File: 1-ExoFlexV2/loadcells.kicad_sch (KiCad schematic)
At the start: 45 parts, among them J70 3,3k, J71 3,3k, J72 0Ω, J73 0Ω, J74 0Ω, J75 0Ω, U13 INA823DR, U14 INA823DR, U15 INA823DR, U19 SN74LVC1G32DBVR, U20 SN74LVC1G32DBVR

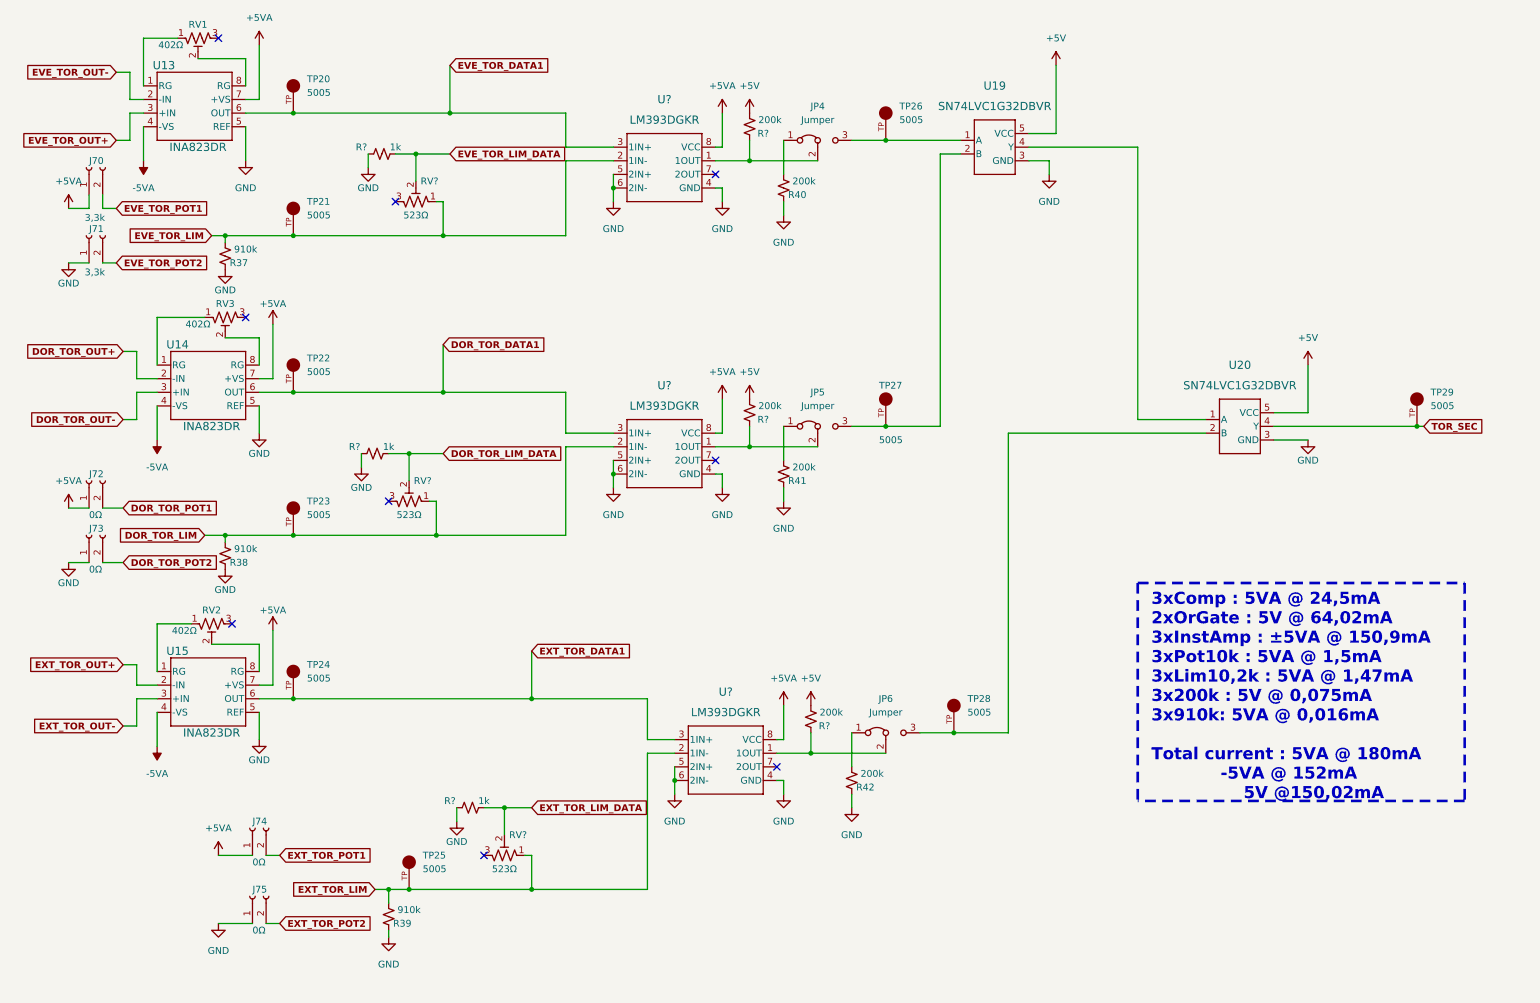
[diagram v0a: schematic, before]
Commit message: Chokes et RC
- Ajout des RF chokes
- Changement des résistance pour 0805
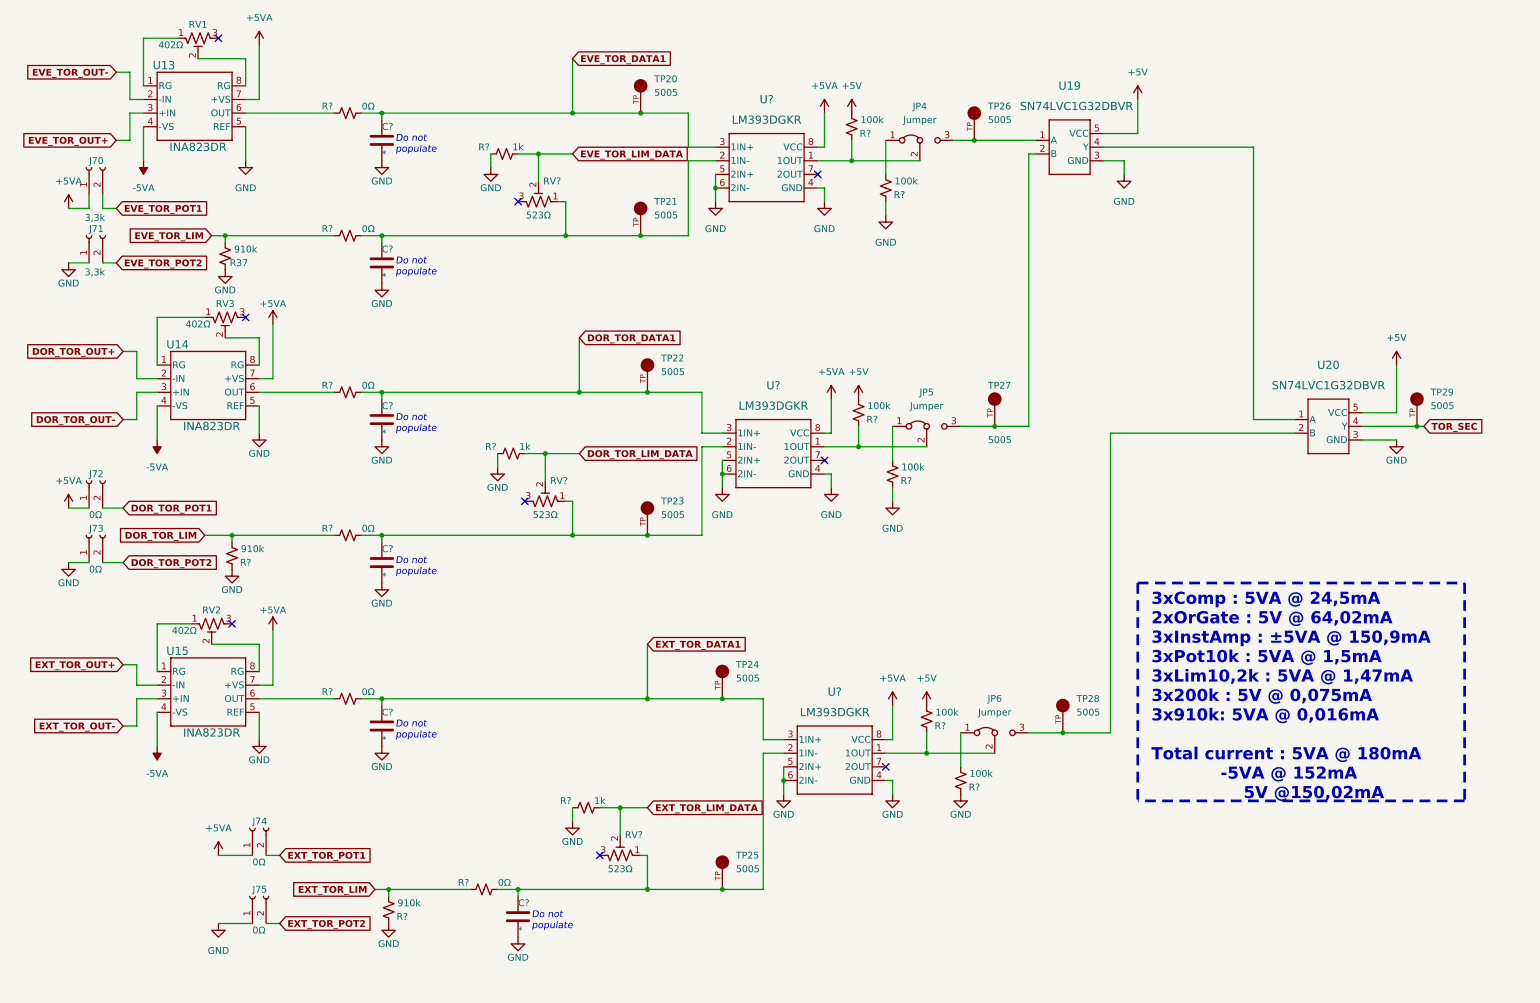
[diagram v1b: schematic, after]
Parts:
- removed R38, R39: 910k, Resistor_SMD:R_0603_1608Metric, symbol Device:R_Small_US
- removed R40, R41, R42, R? (x3): 200k, Resistor_SMD:R_0603_1608Metric, symbol Device:R_Small_US
- added C? (x6): *, Capacitor_SMD:C_0805_2012Metric, symbol Device:C
- added R? (x2): 910k, Resistor_SMD:R_0805_2012Metric, symbol Device:R_Small_US
- added R? (x6): 0Ω, Resistor_SMD:R_0805_2012Metric, symbol Device:R_Small_US
- added R? (x6): 100k, Resistor_SMD:R_0805_2012Metric, symbol Device:R_Small_US
- R37: footprint Resistor_SMD:R_0603_1608Metric -> Resistor_SMD:R_0805_2012Metric
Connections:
- net +5V: now also R?.1, R?.1, R?.1
- net DOR_TOR_DATA1: now also C?.1, R?.2; no longer U14.6 (OUT)
- net DOR_TOR_LIM: now also R?.1, R?.1; no longer RV?.1, TP23.TP, U?.2 (1IN-)
- net EVE_TOR_DATA1: now also C?.1, R?.2; no longer U13.6 (OUT)
- net EVE_TOR_LIM: now also R?.1; no longer RV?.1, TP21.TP, U?.2 (1IN-)
- net EXT_TOR_DATA1: now also C?.1, R?.2; no longer U15.6 (OUT)
- net EXT_TOR_LIM: now also R?.1, R?.1; no longer RV?.1, TP25.TP, U?.2 (1IN-)
- net GND: now also C?.2, C?.2, C?.2, C?.2, C?.2, C?.2, R?.2, R?.2, R?.2, R?.2, R?.2
- net at JP6.1 (A): now also R?.1
- net at JP6.2 (C), U?.1 (1OUT): now also R?.2
- net at JP4.1 (A): now also R?.1
- net at JP4.2 (C), U?.1 (1OUT): now also R?.2
- net at JP5.2 (C), U?.1 (1OUT): now also R?.2
- net at JP5.1 (A): now also R?.1
- new net: C?.1, R?.2, RV?.1, TP21.TP, U?.2 (1IN-)
- new net: R?.1, U14.6 (OUT)
- new net: C?.1, R?.2, RV?.1, TP23.TP, U?.2 (1IN-)
- new net: R?.1, U13.6 (OUT)
- new net: C?.1, R?.2, RV?.1, TP25.TP, U?.2 (1IN-)
- new net: R?.1, U15.6 (OUT)
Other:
- note added: "Do not populate"
- moved on the sheet: JP4, JP5, JP6, R?, RV?, TP20, TP21, TP22, TP23, TP24, TP25, TP26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

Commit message: Trimmer et jumper
-Changement de symbole de jumper
-Ajout des des trimmer aux endroits nécessaires
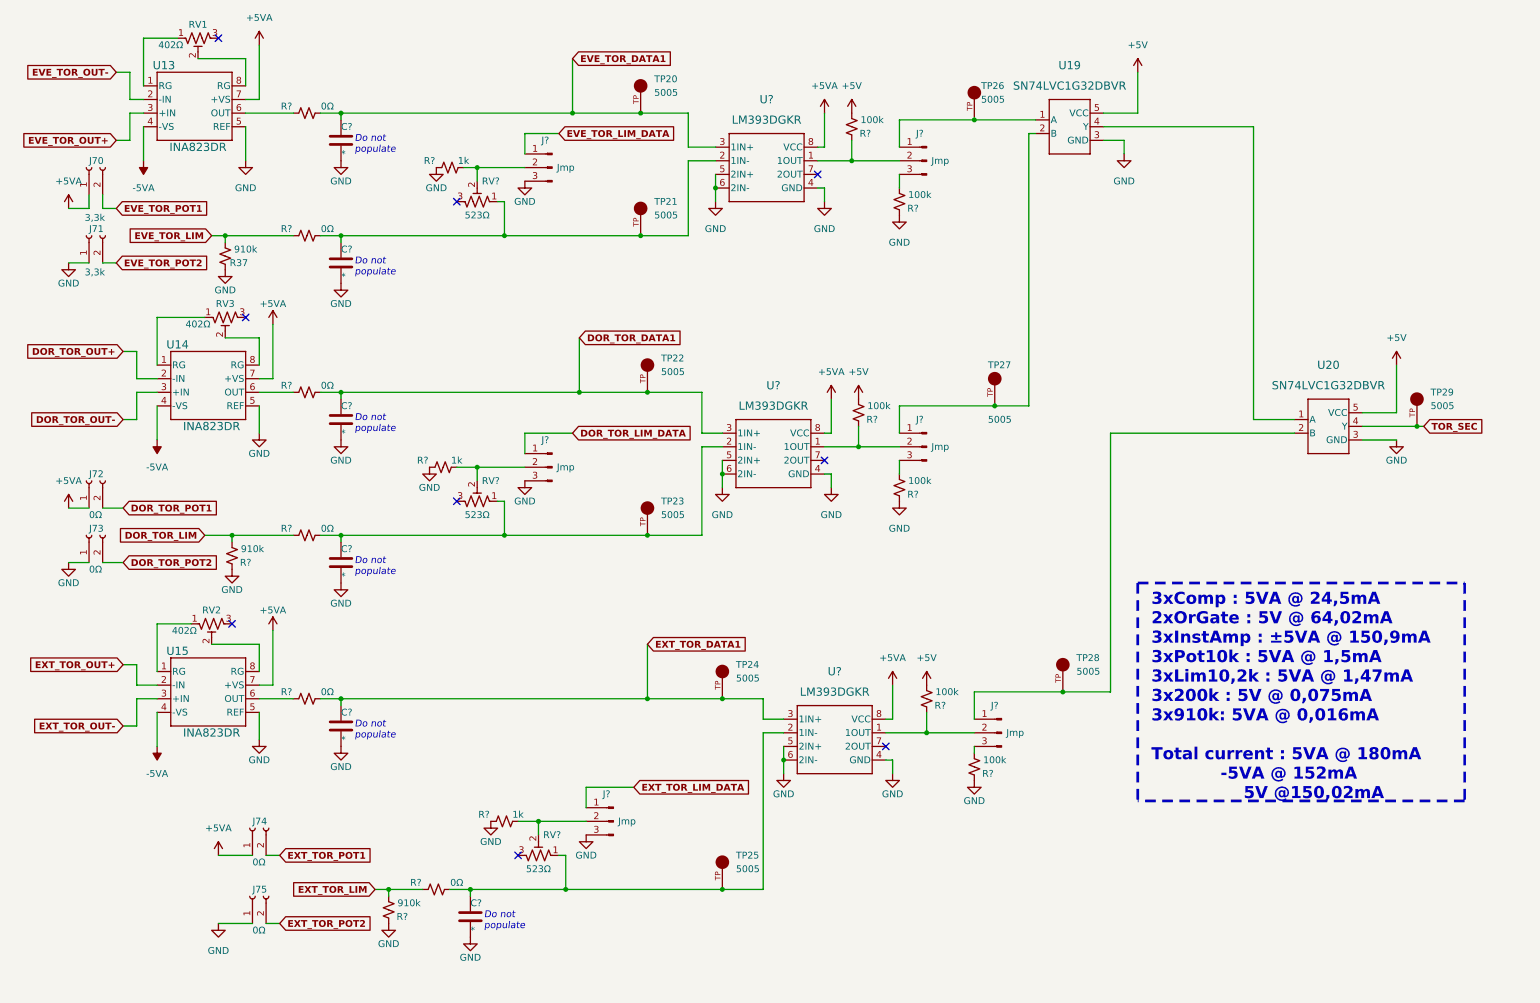
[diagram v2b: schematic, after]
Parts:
- removed JP4, JP5, JP6: Jumper, Connector_PinHeader_2.54mm:PinHeader_1x03_P2.54mm_Vertical, symbol Jumper:Jumper_3_Bridged12
- removed R? (x3): 100k, Resistor_SMD:R_0805_2012Metric, symbol Device:R_Small_US
- removed R?: 1k, Resistor_SMD:R_0805_2012Metric, symbol Device:R_Small_US
- removed RV?: 523Ω, FootPrint:TRIM_3362P-1-102LF, symbol Device:R_Potentiometer_Trim_US
- added J? (x6): Jmp, symbol Connector:Conn_01x03_Male
- added R?: 1k, Resistor_SMD:R_0805_2012Metric, symbol Device:R_Small_US
- added R? (x3): 100k, Resistor_SMD:R_0805_2012Metric, symbol Device:R_Small_US
- added RV?: 523Ω, FootPrint:TRIM_3362P-1-102LF, symbol Device:R_Potentiometer_Trim_US
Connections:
- net DOR_TOR_LIM_DATA: now also J?.1 (Pin_1); no longer R?.2, RV?.2
- net EVE_TOR_LIM_DATA: now also J?.1 (Pin_1); no longer R?.2, RV?.2
- net EXT_TOR_LIM_DATA: now also J?.1 (Pin_1)
- net GND: now also J?.3 (Pin_3), J?.3 (Pin_3), J?.3 (Pin_3), R?.1, R?.2, R?.2, R?.2
- net at TP27.TP, U19.2 (B): now also J?.1 (Pin_1)
- net at R?.2, U?.1 (1OUT): now also J?.2 (Pin_2) (x3)
- net at TP28.TP, U20.2 (B): now also J?.1 (Pin_1)
- net at C?.1, R?.2, TP25.TP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: now also RV?.1
- net at TP26.TP, U19.1 (A): now also J?.1 (Pin_1)
- new net: J?.2 (Pin_2), R?.2, RV?.2 (x3)
- new net: J?.3 (Pin_3), R?.1 (x3)
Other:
- moved on the sheet: C?, R?, RV?, TP26, TP27, TP28, U19, U?

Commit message: Test points et notes
- Ajout de tous les tests point nécessaires
-  Ajoute des sections de notes dans chaque page
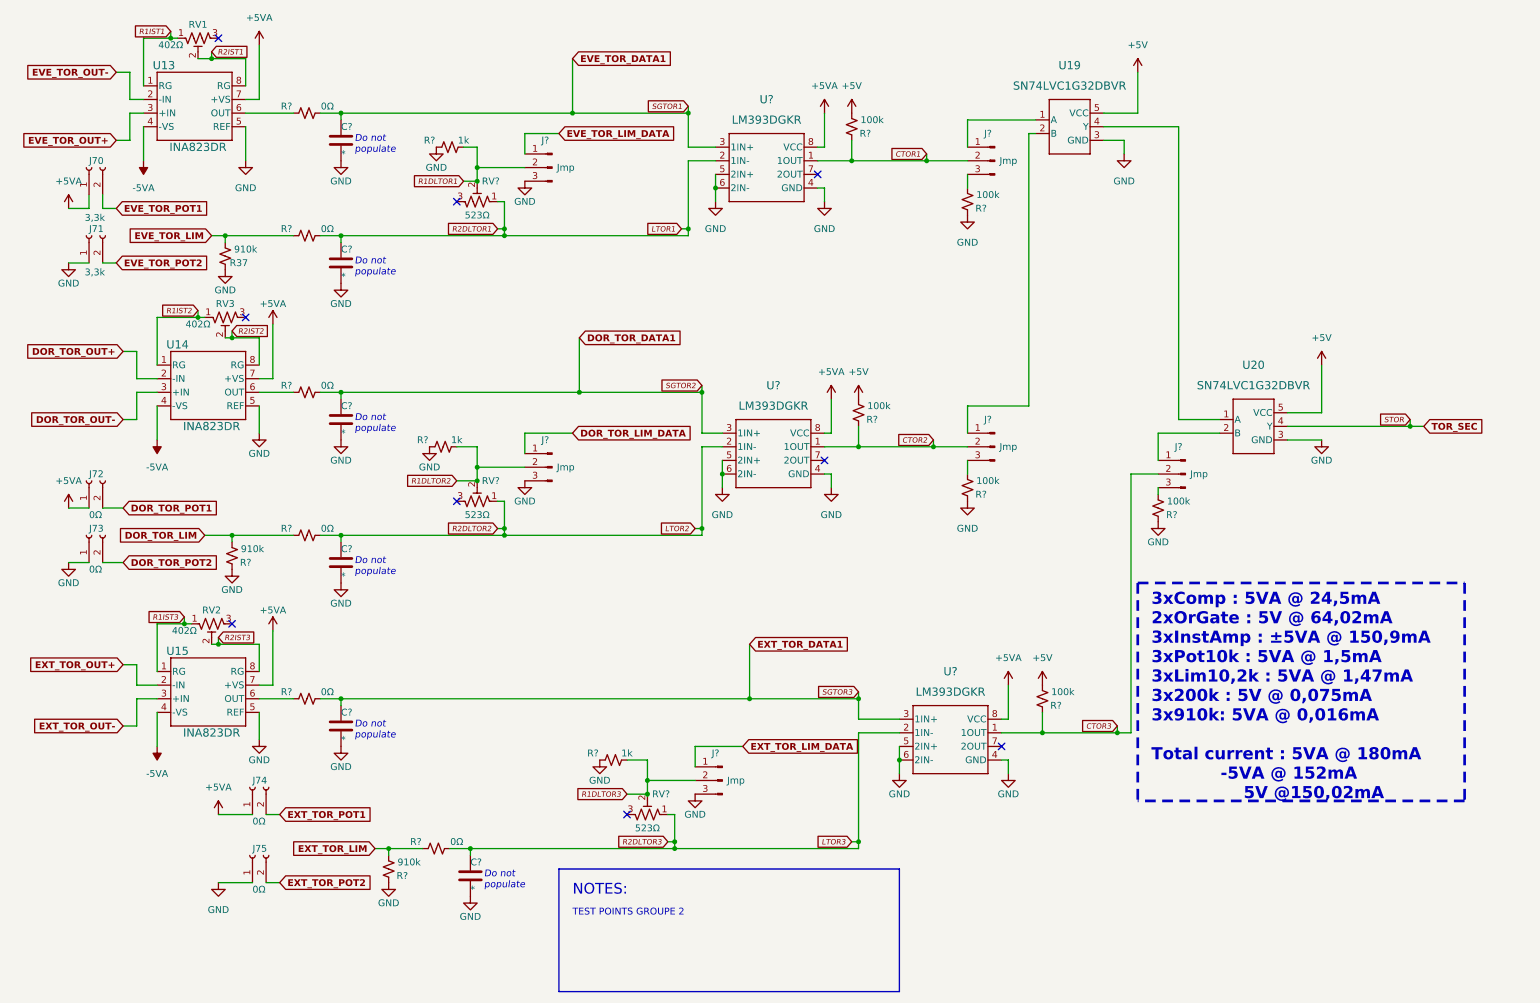
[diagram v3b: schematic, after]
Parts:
- removed TP20, TP21, TP22, TP23, TP24, TP25, TP26, TP27, TP28, TP29: 5005, FootPrint:KEYSTONE_5005, symbol SymLib:5005
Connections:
- net LTOR1: now reaches C?.1, R?.2, RV?.1, U?.2 (1IN-)
- net R1DLTOR1: now reaches J?.2 (Pin_2), R?.2, RV?.2
- net R1DLTOR3: now reaches J?.2 (Pin_2), R?.2, RV?.2
- net R1IST2: now reaches RV3.1, U14.1 (RG)
- net R2IST2: now reaches RV3.2, U14.8 (RG)
- net LTOR2: now reaches C?.1, R?.2, RV?.1, U?.2 (1IN-)
- net CTOR3: now reaches J?.2 (Pin_2), R?.2, U?.1 (1OUT)
- net R1IST1: now reaches RV1.1, U13.1 (RG)
- net R2IST1: now reaches RV1.2, U13.8 (RG)
- net LTOR3: now reaches C?.1, R?.2, RV?.1, U?.2 (1IN-)
- net R1DLTOR2: now reaches J?.2 (Pin_2), R?.2, RV?.2
- net CTOR1: now reaches J?.2 (Pin_2), R?.2, U?.1 (1OUT)
- net CTOR2: now reaches J?.2 (Pin_2), R?.2, U?.1 (1OUT)
- net R1IST3: now reaches RV2.1, U15.1 (RG)
- net R2IST3: now reaches RV2.2, U15.8 (RG)
- net TOR_SEC renamed STOR
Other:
- note added: "NOTES:"
- note added: "TEST POINTS GROUPE 2"
- moved on the sheet: C?, J74, J75, J?, R?, RV?, U20, U?
